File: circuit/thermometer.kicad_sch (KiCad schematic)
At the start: 29 parts, among them IC1 ICL7107CPL, IC2 TMP36, IC3 LM285Z-1.2, IC4 4001, J1 Conn_01x25_Socket, J2 Conn_01x25_Pin

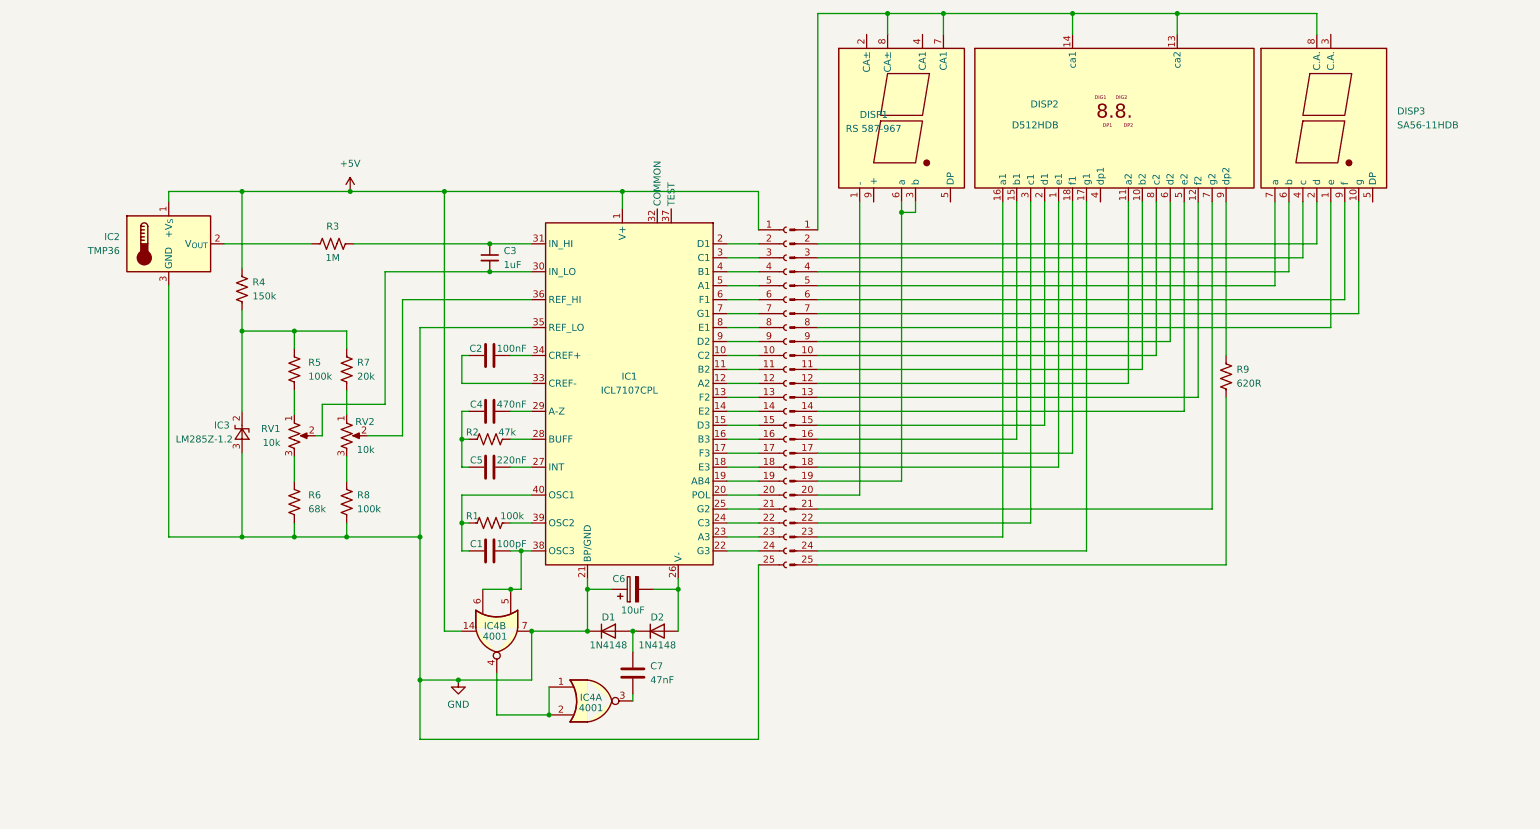
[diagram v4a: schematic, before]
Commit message: Modularise thermometer unit
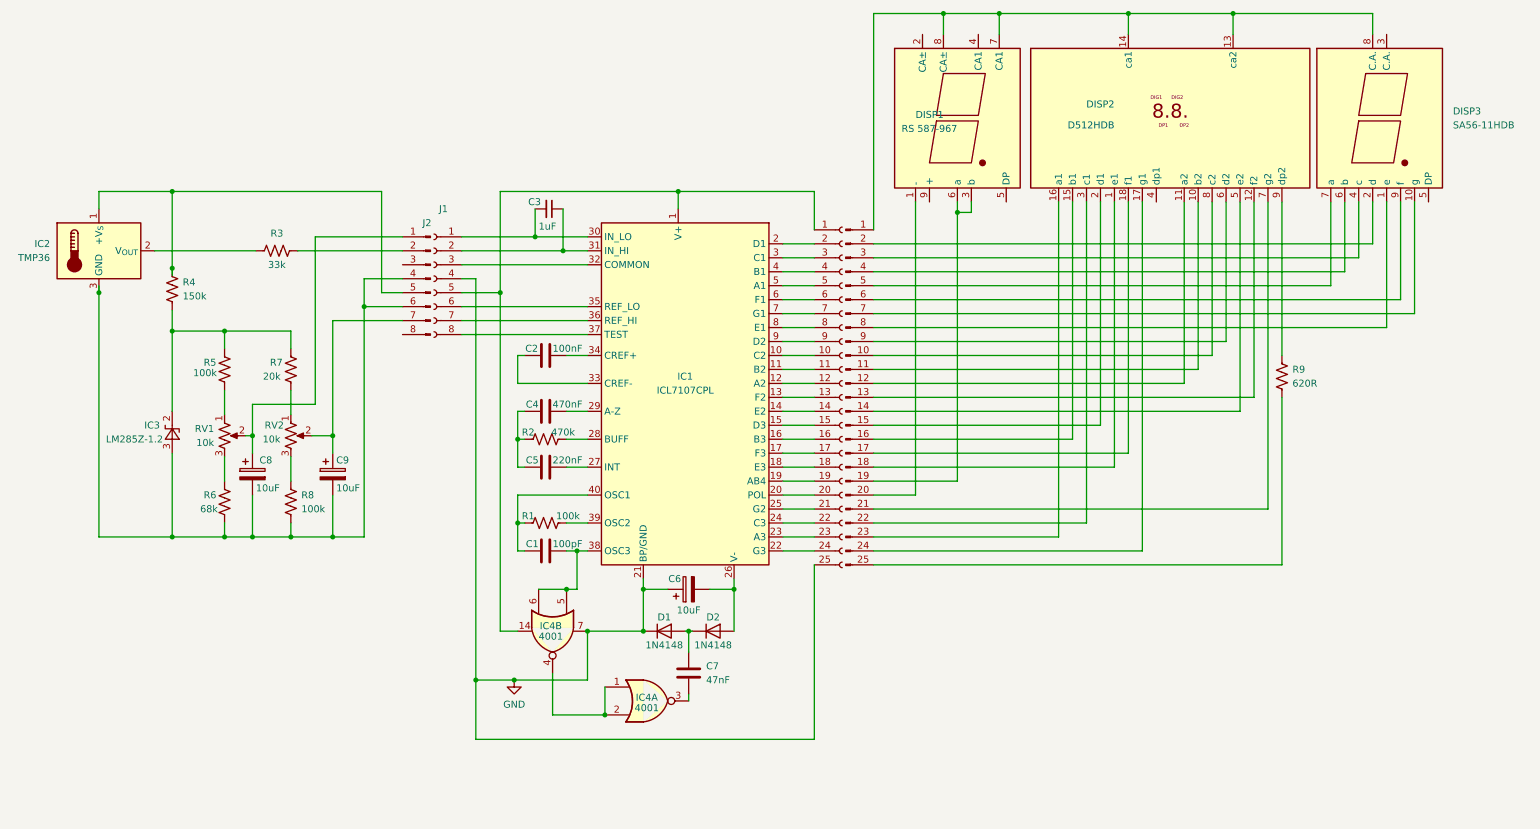
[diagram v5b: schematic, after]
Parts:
- added C8, C9: 10uF, symbol Device:C_Polarized
- added J1: ~, symbol Connector:Conn_01x08_Socket
- added J2: ~, symbol Connector:Conn_01x08_Pin
- R2: value 47k -> 470k
- R3: value 1M -> 33k
- renumbered J1 to J3, J2 to J4
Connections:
- net GND: now also J1.4 (Pin_4); no longer IC1.35 (REF_LO), IC2.3 (GND), IC3.3 (A), R6.2, R8.2
- net at C3.1, IC1.31 (IN_HI): now also J1.2 (Pin_2); no longer R3.2
- net at C3.2, IC1.30 (IN_LO): now also J1.1 (Pin_1); no longer RV1.2
- net at RV2.2: now also C9.1, J2.7 (Pin_7); no longer IC1.36 (REF_HI)
- net at IC1.32 (COMMON): now also J1.3 (Pin_3)
- net at IC1.37 (TEST): now also J1.8 (Pin_8)
- net +5V: no longer names the net of IC1.1 (V+), IC4.14, J3.1 (Pin_1)
- net +5V: now also J1.5 (Pin_5); no longer IC2.1 (+V_{S}), R4.1
- new net: C8.1, J2.1 (Pin_1), RV1.2
- new net: J2.2 (Pin_2), R3.2
- new net: C8.2, C9.2, IC2.3 (GND), IC3.3 (A), J2.4 (Pin_4), J2.6 (Pin_6), R6.2, R8.2
- new net: IC2.1 (+V_{S}), J2.5 (Pin_5), R4.1
- new net: IC1.35 (REF_LO), J1.6 (Pin_6)
- new net: IC1.36 (REF_HI), J1.7 (Pin_7)
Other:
- moved on the sheet: C1, C2, C3, C4, C5, C6, C7, D1, D2, DISP1, DISP2, DISP3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

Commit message: Tying up a few loose ends
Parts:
- removed J3: Conn_01x25_Socket, Connector_PinSocket_2.54mm:PinSocket_1x25_P2.54mm_Vertical, symbol Connector:Conn_01x25_Socket
- removed J4: Conn_01x25_Pin, Connector_PinHeader_2.54mm:PinHeader_1x25_P2.54mm_Vertical, symbol Connector:Conn_01x25_Pin
- added unit 4 of IC4
- added unit 3 of IC4
- added R10: 27k, symbol Device:R_US
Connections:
- net GND: now also R9.2
- net at J2.3 (Pin_3): now also R10.2
- net at IC2.1 (+V_{S}), J2.5 (Pin_5): now also R10.1; no longer R4.1
- net +5V: now reaches IC1.1 (V+), IC4.14, J1.5 (Pin_5)
- net +5V: now also DISP1.7 (CA1), DISP1.8 (CA±), DISP2.13 (ca2), DISP2.14 (ca1), DISP3.8 (C.A.), IC4.12, IC4.13, IC4.8, IC4.9
- net at IC1.10 (C2): now also DISP2.8 (c2)
- net at IC1.11 (B2): now also DISP2.10 (b2)
- net at IC1.12 (A2): now also DISP2.11 (a2)
- net at IC1.13 (F2): now also DISP2.12 (f2)
- net at IC1.14 (E2): now also DISP2.5 (e2)
- net at IC1.15 (D3): now also DISP2.2 (d1)
- net at IC1.16 (B3): now also DISP2.15 (b1)
- net at IC1.17 (F3): now also DISP2.18 (f1)
- net at IC1.18 (E3): now also DISP2.1 (e1)
- net at IC1.19 (AB4): now also DISP1.3 (b), DISP1.6 (a)
- net at IC1.2 (D1): now also DISP3.2 (d)
- net at IC1.20 (POL): now also DISP1.1 (-)
- net at IC1.22 (G3): now also DISP2.17 (g1)
- net at IC1.23 (A3): now also DISP2.16 (a1)
- net at IC1.24 (C3): now also DISP2.3 (c1)
- net at IC1.25 (G2): now also DISP2.7 (g2)
- net at IC1.3 (C1): now also DISP3.4 (c)
- net at IC1.4 (B1): now also DISP3.6 (b)
- net at IC1.5 (A1): now also DISP3.7 (a)
- net at IC1.6 (F1): now also DISP3.9 (f)
- net at IC1.7 (G1): now also DISP3.10 (g)
- net at IC1.8 (E1): now also DISP3.1 (e)
- net at IC1.9 (D2): now also DISP2.6 (d2)
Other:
- note added: "http://ae6pm.com/Application_Notes/Intersil/AN052.pdf"

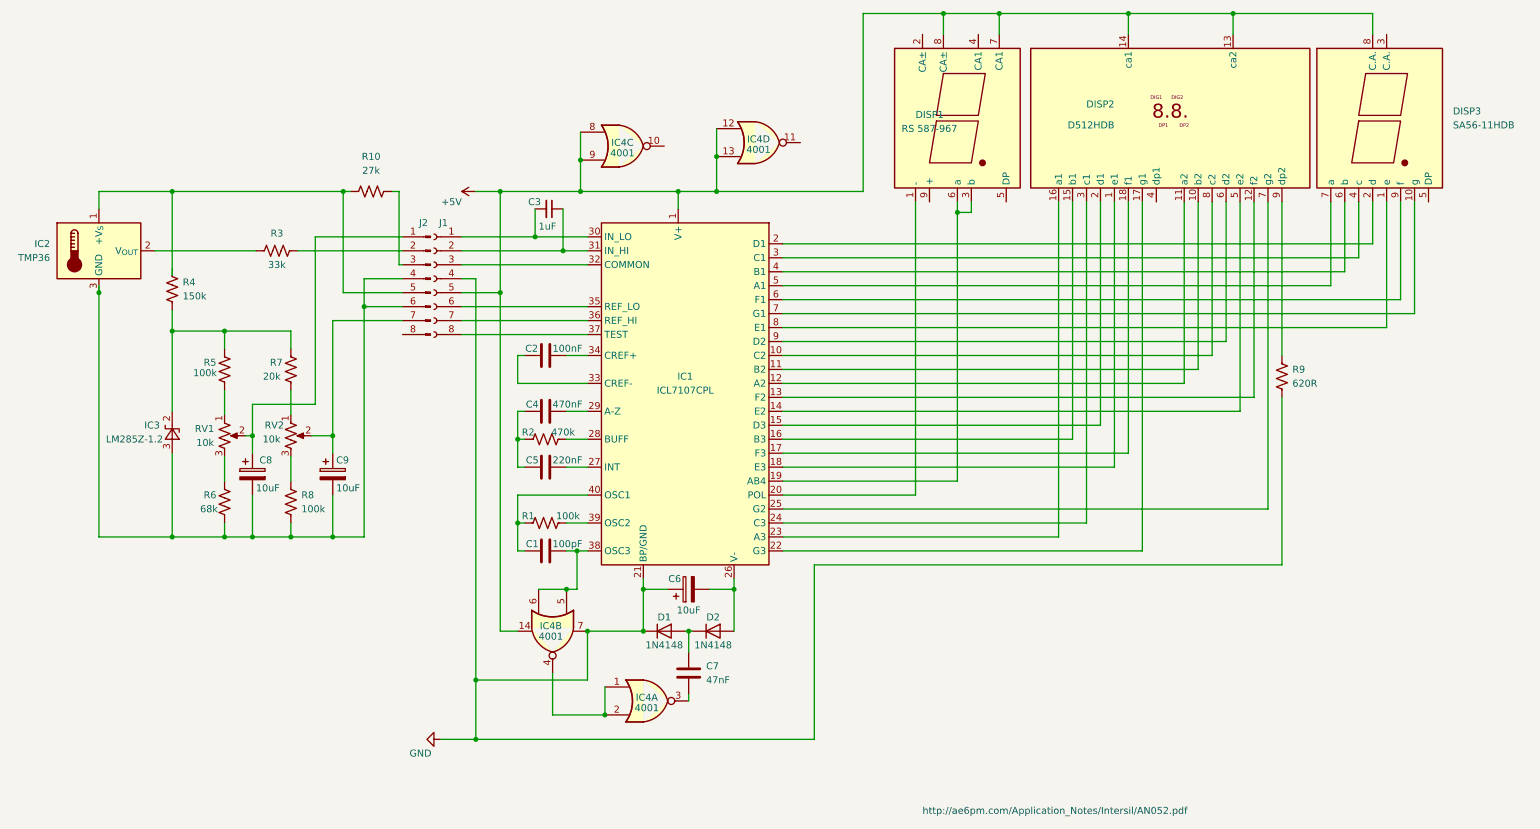
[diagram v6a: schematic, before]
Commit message: Replace display that is no longer available
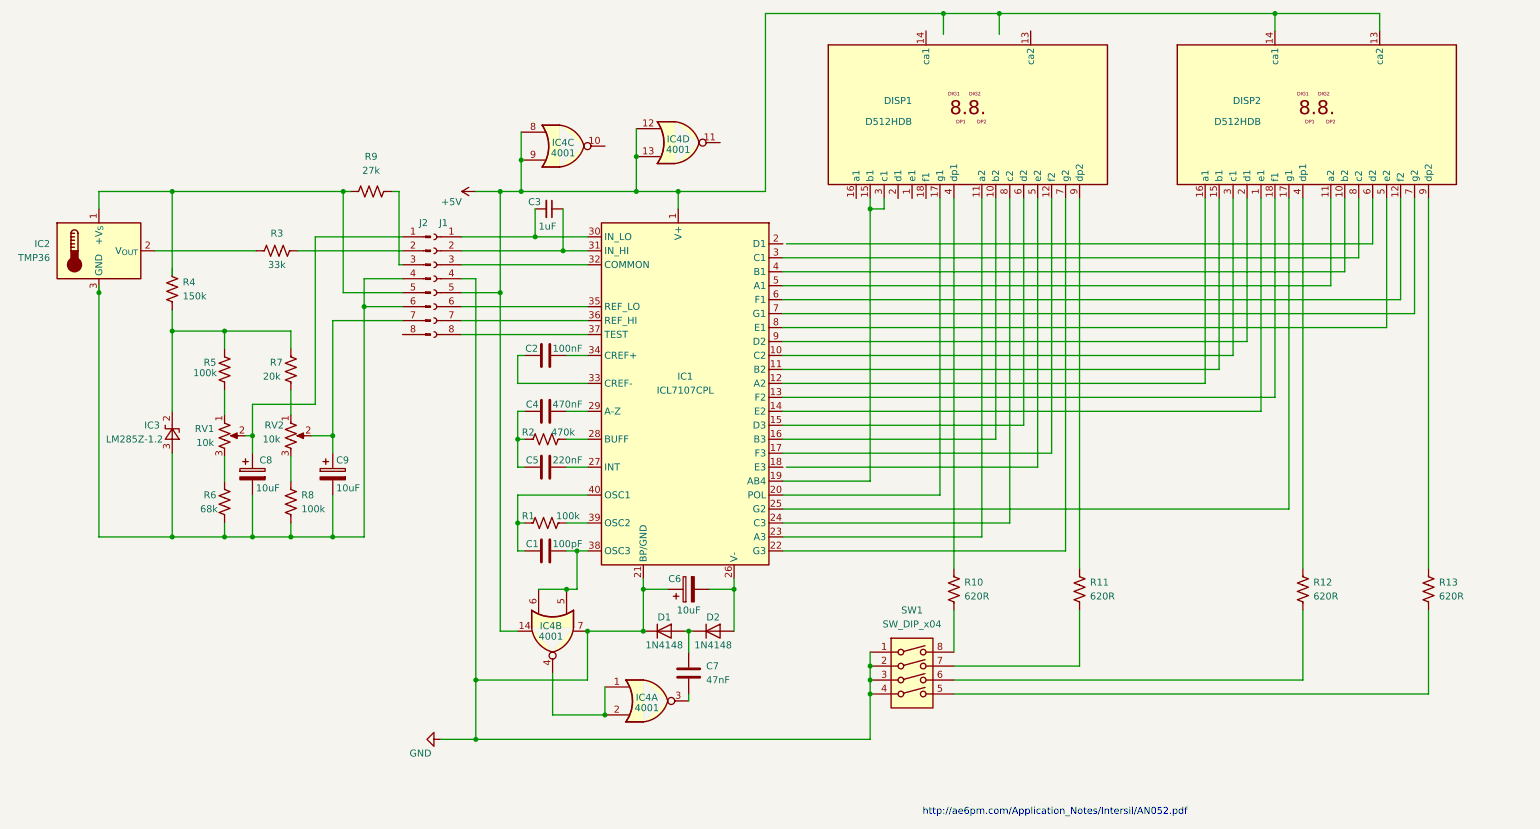
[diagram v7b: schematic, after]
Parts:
- removed DISP1: RS 587-967, Display_7Segment:7SegmentLED_LTS6760_LTS6780, symbol Display_Character:LTS-6960HR
- removed DISP3: SA56-11HDB, Display_7Segment:7SegmentLED_LTS6760_LTS6780, symbol Display_Character:LTS-6960HR
- added DISP1: D512HDB, Display_7Segment:DA56-11SURKWA, symbol Display_Character:DA56-11EWA
- added R11, R12, R13: 620R, Resistor_THT:R_Axial_DIN0204_L3.6mm_D1.6mm_P7.62mm_Horizontal, symbol Device:R_US
- added SW1: SW_DIP_x04, symbol Switch:SW_DIP_x04
- renumbered R9 to R10, R10 to R9
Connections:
- net GND: now also SW1.1, SW1.2, SW1.3, SW1.4; no longer R10.2
- net at IC1.10 (C2): now also DISP2.3 (c1); no longer DISP2.8 (c2)
- net at IC1.11 (B2): now also DISP2.15 (b1); no longer DISP2.10 (b2)
- net at IC1.12 (A2): now also DISP2.16 (a1); no longer DISP2.11 (a2)
- net at IC1.13 (F2): now also DISP2.18 (f1); no longer DISP2.12 (f2)
- net at IC1.14 (E2): now also DISP2.1 (e1); no longer DISP2.5 (e2)
- net at IC1.15 (D3): now also DISP1.6 (d2); no longer DISP2.2 (d1)
- net at IC1.16 (B3): now also DISP1.10 (b2); no longer DISP2.15 (b1)
- net at IC1.17 (F3): now also DISP1.12 (f2); no longer DISP2.18 (f1)
- net at IC1.18 (E3): no longer DISP2.1 (e1)
- net at IC1.19 (AB4): now also DISP1.15 (b1), DISP1.3 (c1)
- net at IC1.20 (POL): now also DISP1.17 (g1)
- net at IC1.22 (G3): now also DISP1.7 (g2); no longer DISP2.17 (g1)
- net at IC1.23 (A3): now also DISP1.11 (a2); no longer DISP2.16 (a1)
- net at IC1.24 (C3): now also DISP1.8 (c2); no longer DISP2.3 (c1)
- net at IC1.25 (G2): now also DISP2.17 (g1); no longer DISP2.7 (g2)
- net at IC1.3 (C1): now also DISP2.8 (c2)
- net at IC1.4 (B1): now also DISP2.10 (b2)
- net at IC1.5 (A1): now also DISP2.11 (a2)
- net at IC1.6 (F1): now also DISP2.12 (f2)
- net at IC1.7 (G1): now also DISP2.7 (g2)
- net at IC1.8 (E1): now also DISP2.5 (e2)
- net at IC1.9 (D2): now also DISP2.2 (d1); no longer DISP2.6 (d2)
- net at R10.1: now also SW1.8; no longer DISP2.9 (dp2)
- net at DISP2.4 (dp1): now also R12.1
- new net: R12.2, SW1.6
- new net: R13.2, SW1.5
- new net: R11.2, SW1.7
- new net: DISP1.4 (dp1), R10.2
- new net: DISP1.9 (dp2), R11.1
- new net: DISP2.9 (dp2), R13.1
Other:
- moved on the sheet: DISP2, IC4C, IC4D, R10

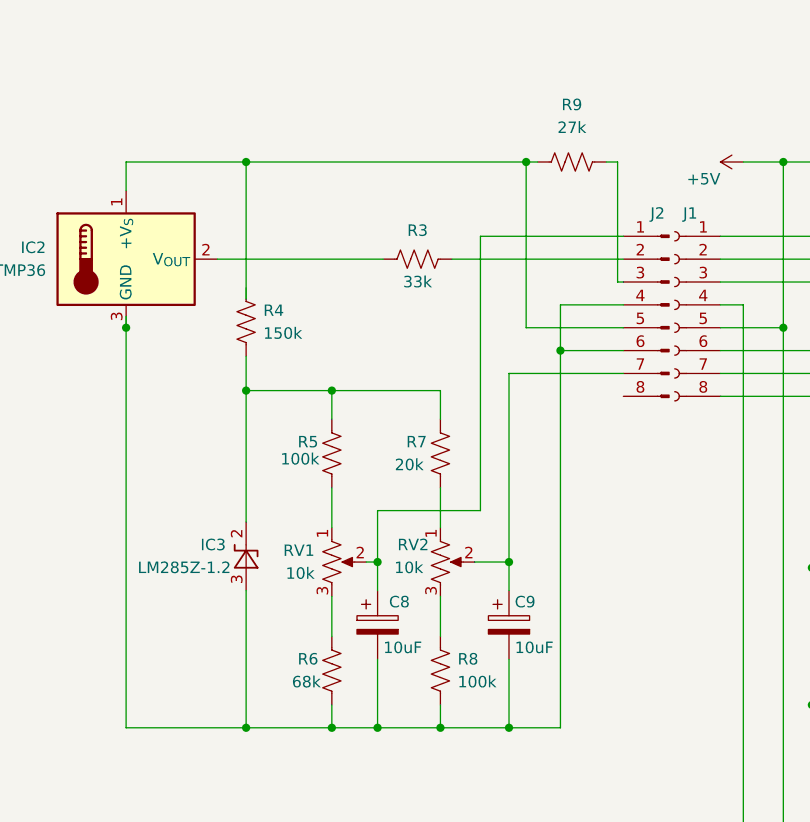
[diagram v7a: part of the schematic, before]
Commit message: PCB for the thermoboard module
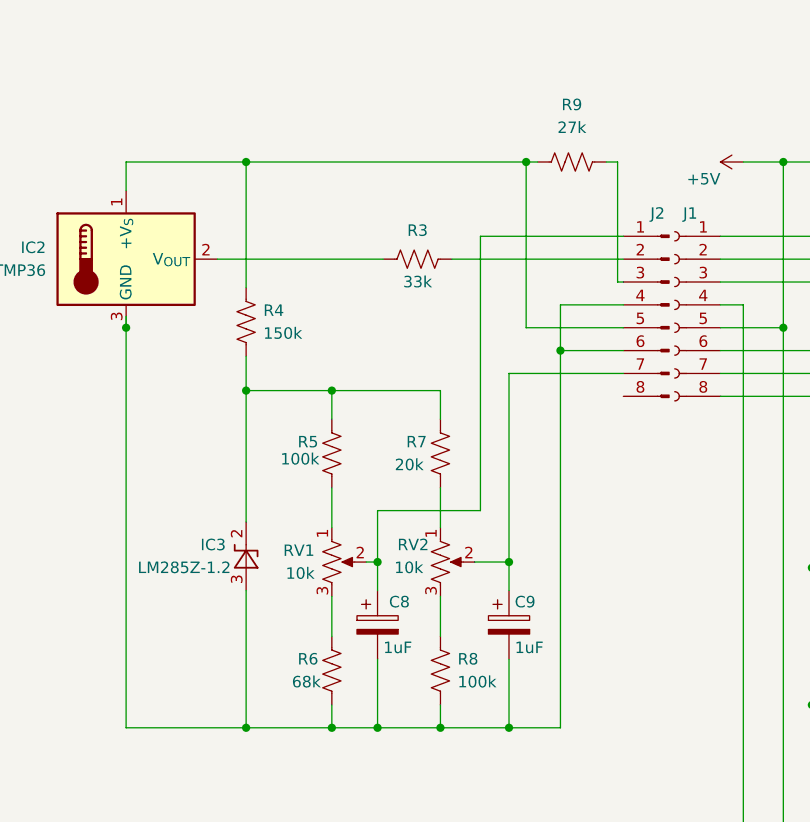
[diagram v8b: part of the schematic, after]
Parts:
- C8, C9: value 10uF -> 1uF; footprint (none) -> Capacitor_THT:CP_Radial_D5.0mm_P2.50mm
- IC2, IC3: footprint Package_TO_SOT_THT:TO-92_Inline -> Package_TO_SOT_THT:TO-92L_Inline_Wide
- J1: footprint (none) -> Connector_PinSocket_2.54mm:PinSocket_1x08_P2.54mm_Vertical
- J2: footprint (none) -> Connector_PinHeader_2.54mm:PinHeader_1x08_P2.54mm_Vertical
- R9: footprint (none) -> Resistor_THT:R_Axial_DIN0204_L3.6mm_D1.6mm_P7.62mm_Horizontal
- RV1, RV2: footprint Potentiometer_THT:Potentiometer_Piher_PT-6-V_Vertical -> Potentiometer_THT:Potentiometer_Bourns_3266Y_Vertical
- SW1: footprint (none) -> Button_Switch_THT:SW_DIP_SPSTx04_Slide_9.78x12.34mm_W7.62mm_P2.54mm
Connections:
- net at IC2.1 (+V_{S}), J2.5 (Pin_5), R9.1: now also R4.1
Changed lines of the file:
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@@
     (stroke (width 0) (type default))
   )
-  (wire (pts (xy 42.545 57.15) (xy 42.545 72.39))
+  (wire (pts (xy 42.545 57.15) (xy 42.545 71.12))
     (stroke (width 0) (type default))
   )
@@
       (effects (font (size 1.27 1.27)))
     )
-    (property "Footprint" "" (at 177.165 146.05 0)
+    (property "Footprint" "Button_Switch_THT:SW_DIP_SPSTx04_Slide_9.78x12.34mm_W7.62mm_P2.54mm" (at 177.165 146.05 0)
       (effects (font (size 1.27 1.27)) hide)
     )
@@
       (effects (font (size 1.27 1.27)))
     )
-    (property "Footprint" "" (at 89.535 73.025 0)
+    (property "Footprint" "Connector_PinHeader_2.54mm:PinHeader_1x08_P2.54mm_Vertical" (at 89.535 73.025 0)
       (effects (font (size 1.27 1.27)) hide)
     )
@@
       (effects (font (size 1.27 1.27)) (justify right))
     )
-    (property "Footprint" "Potentiometer_THT:Potentiometer_Piher_PT-6-V_Vertical" (at 64.135 101.6 0)
+    (property "Footprint" "Potentiometer_THT:Potentiometer_Bourns_3266Y_Vertical" (at 64.135 101.6 0)
       (effects (font (size 1.27 1.27)) hide)
     )
@@
       (effects (font (size 1.27 1.27)))
     )
-    (property "Footprint" "" (at 78.994 56.134 90)
+    (property "Footprint" "Resistor_THT:R_Axial_DIN0204_L3.6mm_D1.6mm_P7.62mm_Horizontal" (at 78.994 56.134 90)
       (effects (font (size 1.27 1.27)) hide)
     )
@@
       (effects (font (size 1.27 1.27)) (justify right))
     )
-    (property "Footprint" "Package_TO_SOT_THT:TO-92_Inline" (at 30.48 74.295 0)
+    (property "Footprint" "Package_TO_SOT_THT:TO-92L_Inline_Wide" (at 30.48 74.295 0)
       (effects (font (size 1.27 1.27)) (justify left) hide)
     )
@@
       (effects (font (size 1.27 1.27)) (justify right))
     )
-    (property "Footprint" "Potentiometer_THT:Potentiometer_Piher_PT-6-V_Vertical" (at 52.07 101.6 0)
+    (property "Footprint" "Potentiometer_THT:Potentiometer_Bourns_3266Y_Vertical" (at 52.07 101.6 0)
       (effects (font (size 1.27 1.27)) hide)
     )
@@
       (effects (font (size 1.27 1.27)) (justify left))
     )
-    (property "Value" "10uF" (at 57.785 111.125 0)
-      (effects (font (size 1.27 1.27)) (justify left))
-    )
-    (property "Footprint" "" (at 58.1152 112.395 0)
+    (property "Value" "1uF" (at 57.785 111.125 0)
+      (effects (font (size 1.27 1.27)) (justify left))
+    )
+    (property "Footprint" "Capacitor_THT:CP_Radial_D5.0mm_P2.50mm" (at 58.1152 112.395 0)
       (effects (font (size 1.27 1.27)) hide)
     )
@@
       (effects (font (size 1.27 1.27)) (justify left))
     )
-    (property "Value" "10uF" (at 72.39 111.125 0)
-      (effects (font (size 1.27 1.27)) (justify left))
-    )
-    (property "Footprint" "" (at 72.7202 112.395 0)
+    (property "Value" "1uF" (at 72.39 111.125 0)
+      (effects (font (size 1.27 1.27)) (justify left))
+    )
+    (property "Footprint" "Capacitor_THT:CP_Radial_D5.0mm_P2.50mm" (at 72.7202 112.395 0)
       (effects (font (size 1.27 1.27)) hide)
     )
@@
       (effects (font (size 1.27 1.27)) (justify right))
     )
-    (property "Footprint" "" (at 90.17 73.025 0)
+    (property "Footprint" "Connector_PinSocket_2.54mm:PinSocket_1x08_P2.54mm_Vertical" (at 90.17 73.025 0)
       (effects (font (size 1.27 1.27)) hide)
     )
@@
       (effects (font (size 1.27 1.27)) (justify right))
     )
-    (property "Footprint" "Package_TO_SOT_THT:TO-92_Inline" (at 47.625 100.965 0)
+    (property "Footprint" "Package_TO_SOT_THT:TO-92L_Inline_Wide" (at 47.625 100.965 0)
       (effects (font (size 1.27 1.27) italic) hide)
     )
